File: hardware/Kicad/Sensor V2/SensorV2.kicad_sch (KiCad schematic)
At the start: 16 parts, among them J1 Controller Connector, J2 Conn_01x08, J3 Conn_01x08, J4 Conn_01x06, J5 Conn_01x06, J6 Conn_01x04, U1 2821, U4 MicroSD_Breakout

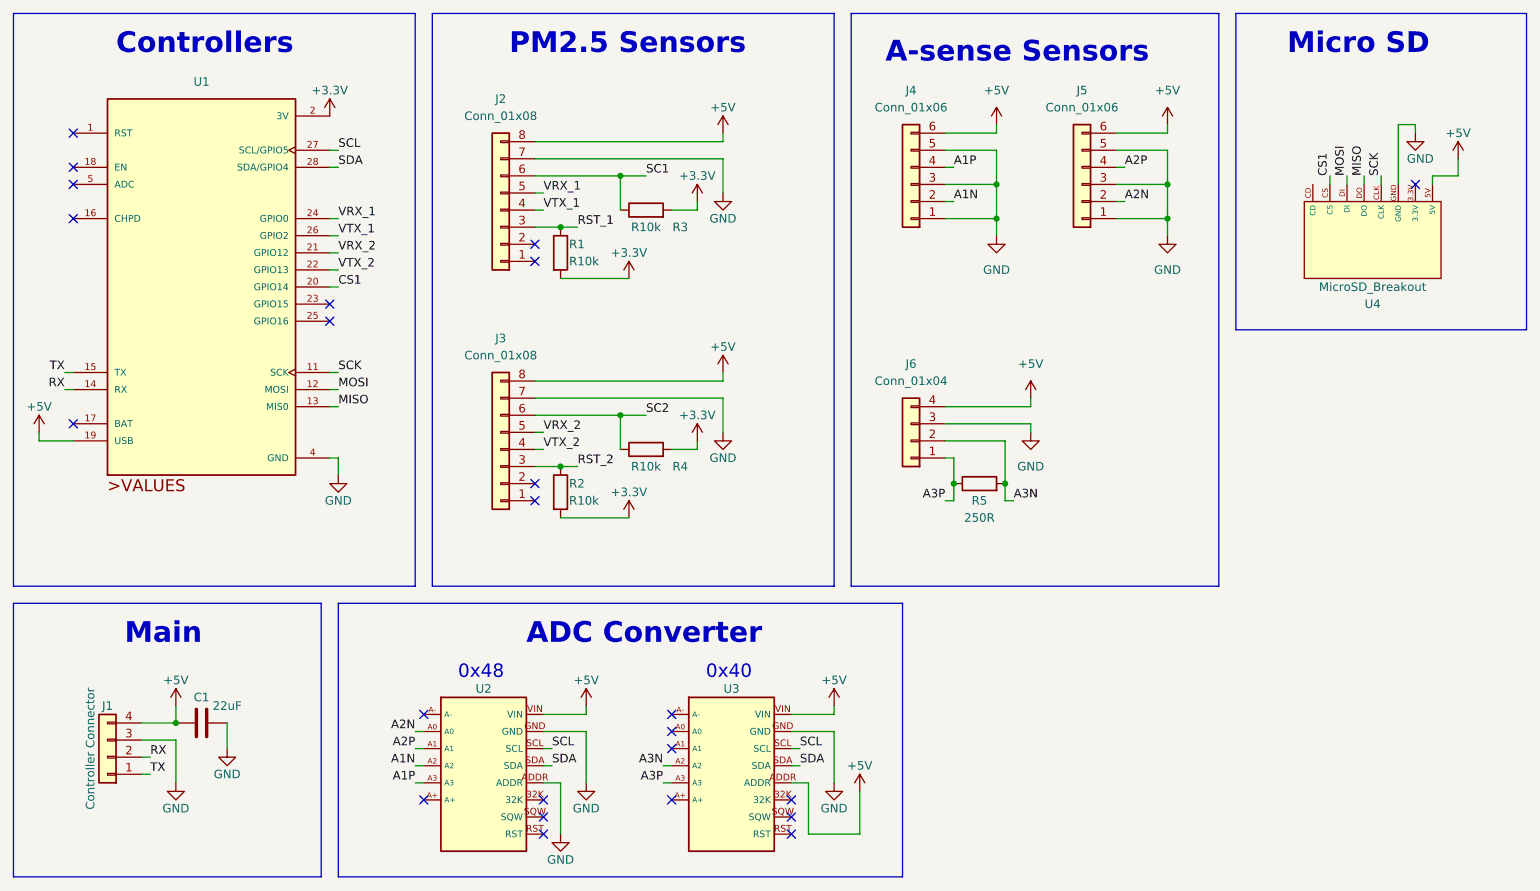
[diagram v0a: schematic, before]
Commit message: fixed CS to gpio16
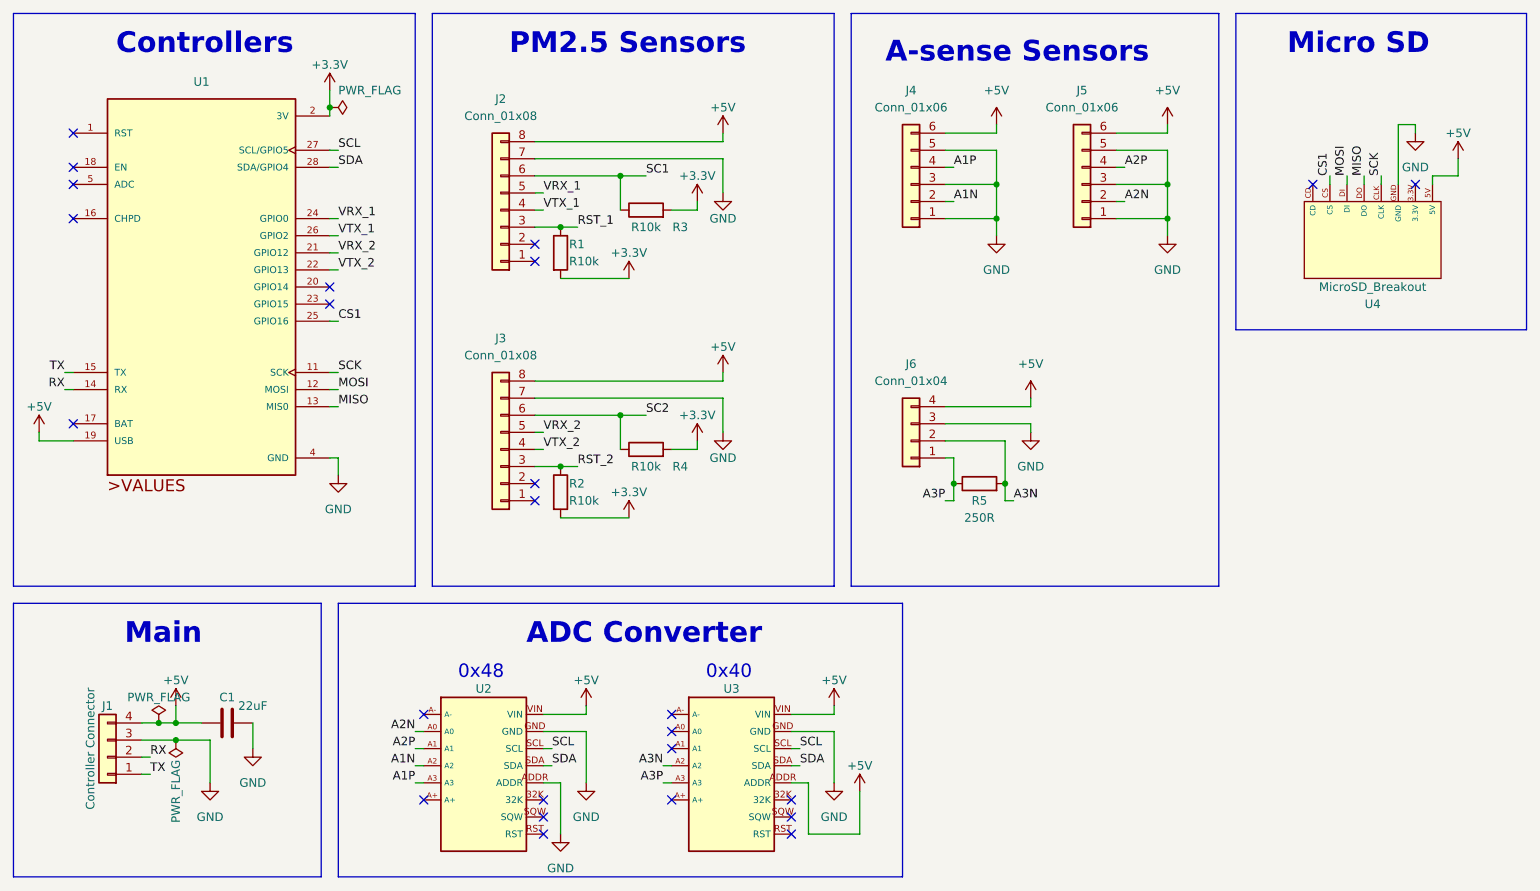
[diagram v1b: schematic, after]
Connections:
- net CS1: now also U1.25 (GPIO16); no longer U1.20 (GPIO14)
- no-connect marks 24 -> 25
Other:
- moved on the sheet: C1

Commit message: added some changes
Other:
- note added: "0x49"
- note removed: "0x40"
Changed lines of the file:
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@@
     (effects (font (size 3.08 3.08) (thickness 0.616) bold) (justify left bottom))
   )
-  (text "0x40\n" (at 116.84 113.03 0)
+  (text "0x49\n" (at 116.84 113.03 0)
     (effects (font (size 2 2)) (justify left bottom))
   )

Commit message: more PCB updates
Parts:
- removed U2: ~, Adafruit_Sensors:ADCRTC_Dual, symbol Adafruit_Files:ADC/RTC_Dual
- added U5: 4Channel_ADC_Breakout, Adafruit_Sensors:4Channel ADC Breakout, symbol Adafruit_Files:4Channel_ADC_Breakout
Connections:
- net +5V: now also U5.VIN
- net A1N: now also U5.A2
- net A1P: now also U5.A3
- net A2N: now also U5.A0
- net A2P: now also U5.A1
- net GND: now also U5.ADDR, U5.GND
- net SCL: now also U5.SCL
- net SDA: now also U5.SDA
- no-connect marks 25 -> 23
